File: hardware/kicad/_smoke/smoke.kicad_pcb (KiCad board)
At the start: 2 copper layers, 50 x 30 mm, 1 part

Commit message: hardware: CP3 iter 2 — project-local footprint cache (Finding 01)
Codex iter-1 finding: host-path footprint loading is non-reproducible.
Fix mirrors CP2 symbol-library pattern.

- hardware/kicad/build_pcbs.py: resolves footprints only from
  hardware/kicad/libraries/volthium.pretty/; never reads host KiCad
  paths during a default build.
- --rebuild-footprints flag is the single code path that touches the
  host KiCad footprint tree (extracts STOCK_FOOTPRINTS list into the
  project cache).
- libraries/volthium.pretty/ seeded with R_0805_2012Metric.kicad_mod
  (smoke test's only footprint). Full audit + cache population of
  all CP2 footprints starts at iter 3.
- Smoke PCB libId switched to volthium:R_0805_2012Metric.
- hardware/kicad/_smoke/fp-lib-table declares the volthium nickname
  via ${KIPRJMOD}/../libraries/volthium.pretty. Pattern repeats per
  board at iter 3.
- cp3_placement.md §3 rewritten; §10.2 designer response added.

Re-ran smoke test from project-local cache only:
- 0 errors, 0 unconnected items, 0 footprint errors
- 3 silk-overlap warnings (cosmetic REF** placeholder; gone after
  real placement)
- no lib_footprint_issues (fp-lib-table resolved it)
- smoke.kicad_pcb has 'volthium:R_0805_2012Metric' libId

SEMAPHORE -> codex_turn iter 3.

Co-Authored-By: Claude Opus 4.7 (1M context) <noreply@anthropic.com>
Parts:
- removed the REF** at (25.0, 15.0)
- added REF**: R_0805_2012Metric, volthium:R_0805_2012Metric, F.Cu at (25.0, 15.0)
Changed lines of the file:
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@@
 		)
 	)
-	(footprint "Resistor_SMD:R_0805_2012Metric"
+	(footprint "volthium:R_0805_2012Metric"
 		(layer "F.Cu")
 		(at 25 15)

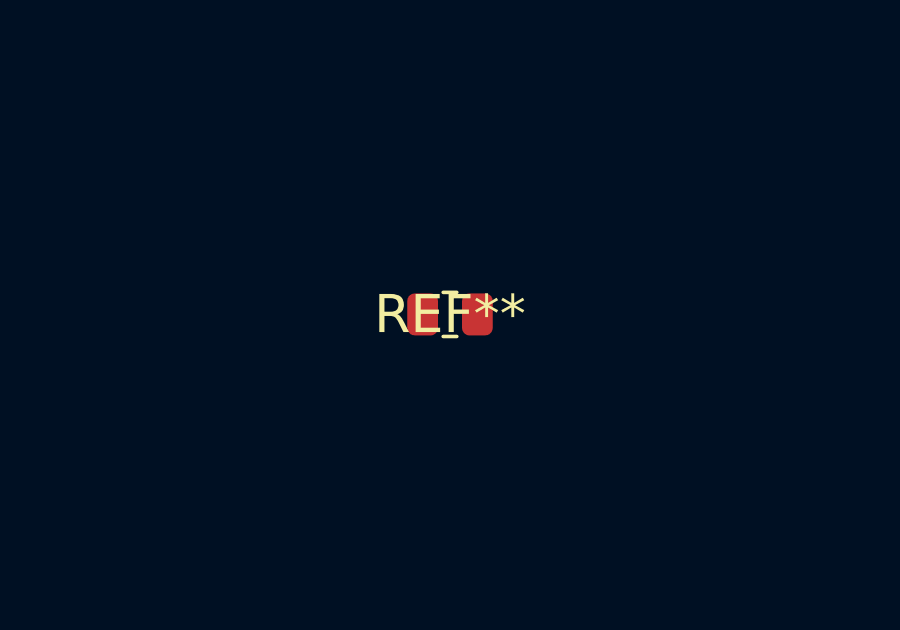
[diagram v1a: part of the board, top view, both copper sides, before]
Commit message: hardware: CP3 iter 4 — footprint audit + cache population (22/22 hits)
Per CP3 plan §6, this iter completes the footprint audit step.

Audit method: walk both CP2 netlists (battery_side.net,
display_side.net), extract every (footprint "lib:name") reference,
check each against KiCad 10 stock libraries.

Result: 23 unique footprint references, 17 hit stock directly, 6
needed schematic-source corrections:

1. Package_SO:SOT-23-6 -> Package_TO_SOT_SMD:SOT-23-6 (wrong namespace)
2. RF_Module:ESP32-S2-WROOM-1 -> RF_Module:ESP32-S3-WROOM-1 (typo)
3. Battery:BatteryHolder_Keystone_1066_1x12mm -> Battery:BatteryHolder_Keystone_1057_1x2032
4. Button_Switch_SMD:SW_SPST_TL3300 -> Button_Switch_SMD:SW_SPST_B3S-1000
5. Converter_DCDC:R-78E-1.0_THT -> Converter_DCDC:R-78E-0.5_THT (same Recom body)
6. Fuse:Fuse_Bel_5MF -> Fuse:Fuseholder_Clip-5x20mm_Bel_FC-203-22_Lateral_...
   (canonical KiCad name for the same Bel cartridge clip family)

All fixes applied at the schematic source in build_schematics.py
(STOCK_SYMBOLS Footprint fields). Schematics regenerated and ERC
remains 0 errors / 0 warnings on both boards. Net topology
unchanged — these are metadata strings, not pin connections.

After fixes: 22 unique footprints (one collapse: both Recom modules
now share the R-78E-0.5_THT footprint). 22/22 hit KiCad stock — no
hand-authored footprints needed.

build_pcbs.py STOCK_FOOTPRINTS now lists all 22; --rebuild-footprints
populates volthium.pretty/ with the corresponding .kicad_mod files
(committed in this commit).

cp3_placement.md §10.4 has the full audit table + per-component
disposition list.

SEMAPHORE -> codex_turn iter 5.

Also: gitignore .DS_Store to keep macOS Finder cruft out of the tree.

Co-Authored-By: Claude Opus 4.7 (1M context) <noreply@anthropic.com>
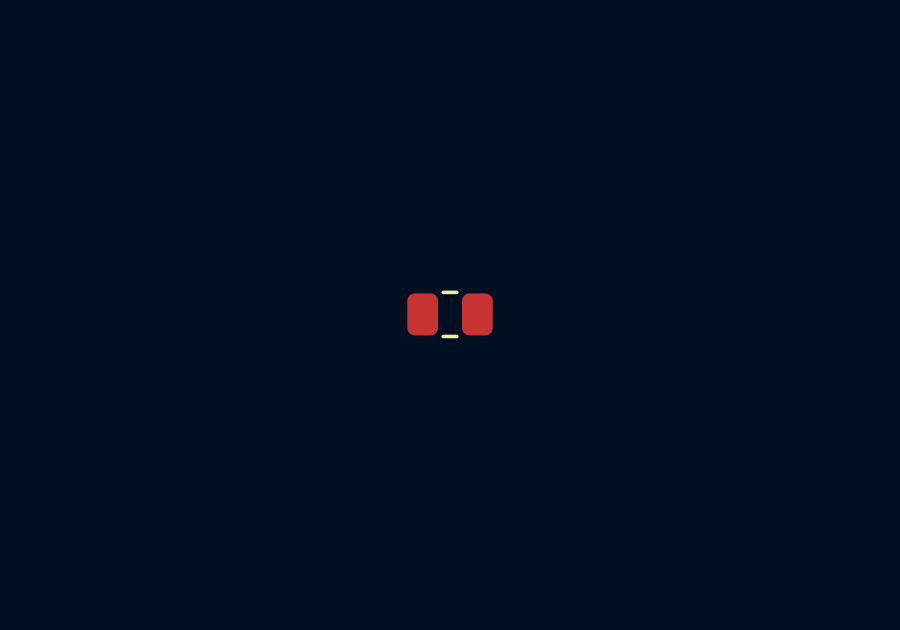
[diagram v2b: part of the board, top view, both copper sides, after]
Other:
- rule pad_to_mask_clearance: 0 -> 0.0
